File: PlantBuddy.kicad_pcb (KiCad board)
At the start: 4 copper layers, 44.3 x 29.2 mm, 75 parts, among them J1 USB_C_Receptacle_USB2.0, J101 JST, J102 J-Link SWD, J4 External, Q101 DMG1012T, SW1 SW_Push, U1 LTR-303ALS-01, U101 RT9080-33GJ5, U102 nRF52832-QFAA, U104 XB5350A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

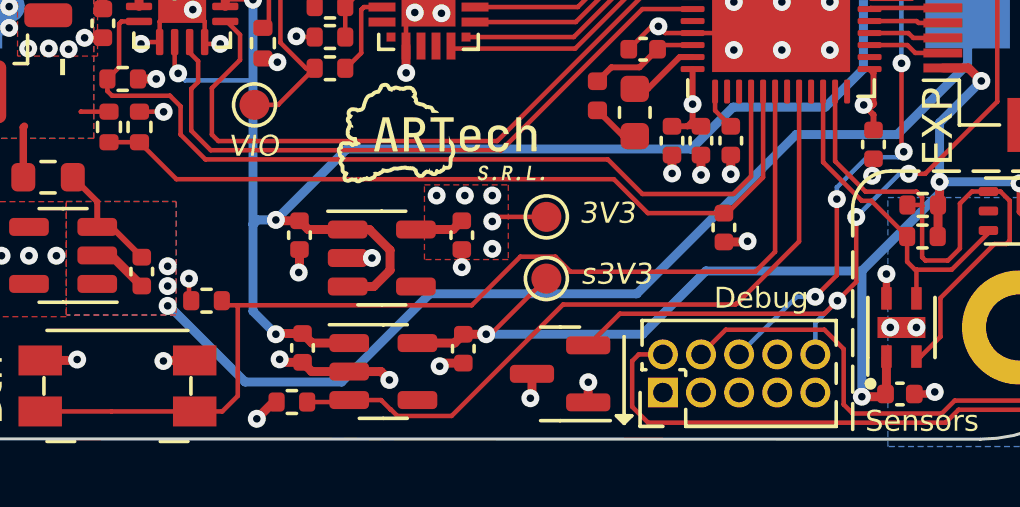
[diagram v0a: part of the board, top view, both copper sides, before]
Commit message: Added voltage monitoring IC. Shuts everything down if Vbat < 3V
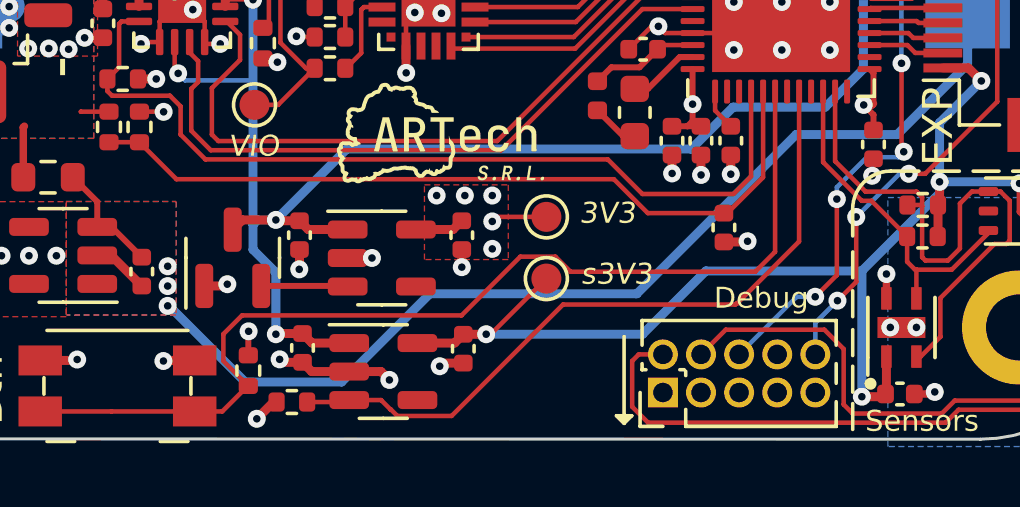
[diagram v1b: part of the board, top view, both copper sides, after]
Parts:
- U105: value CN809R -> CN809T
- moved U105 11.6 mm to (130.2, 136.0), turned to 90 degrees
- moved R108 2.72 mm to (130.7, 139.8), turned to 90 degrees
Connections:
- U105 pad 2: /~{tRST} -> /PWR_EN
- U105 pad 3: +3V3 -> VCC
- U5 pad 3: VCC -> /PWR_EN
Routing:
- net /~{tRST}: track 30.9 -> 21.9 mm
- net /PWR_EN: track 0.00 -> 2.89 mm
- net VCC: track 62.8 -> 60.4 mm
- net +3V3: track 15.3 -> 14.5 mm, vias 10 -> 9

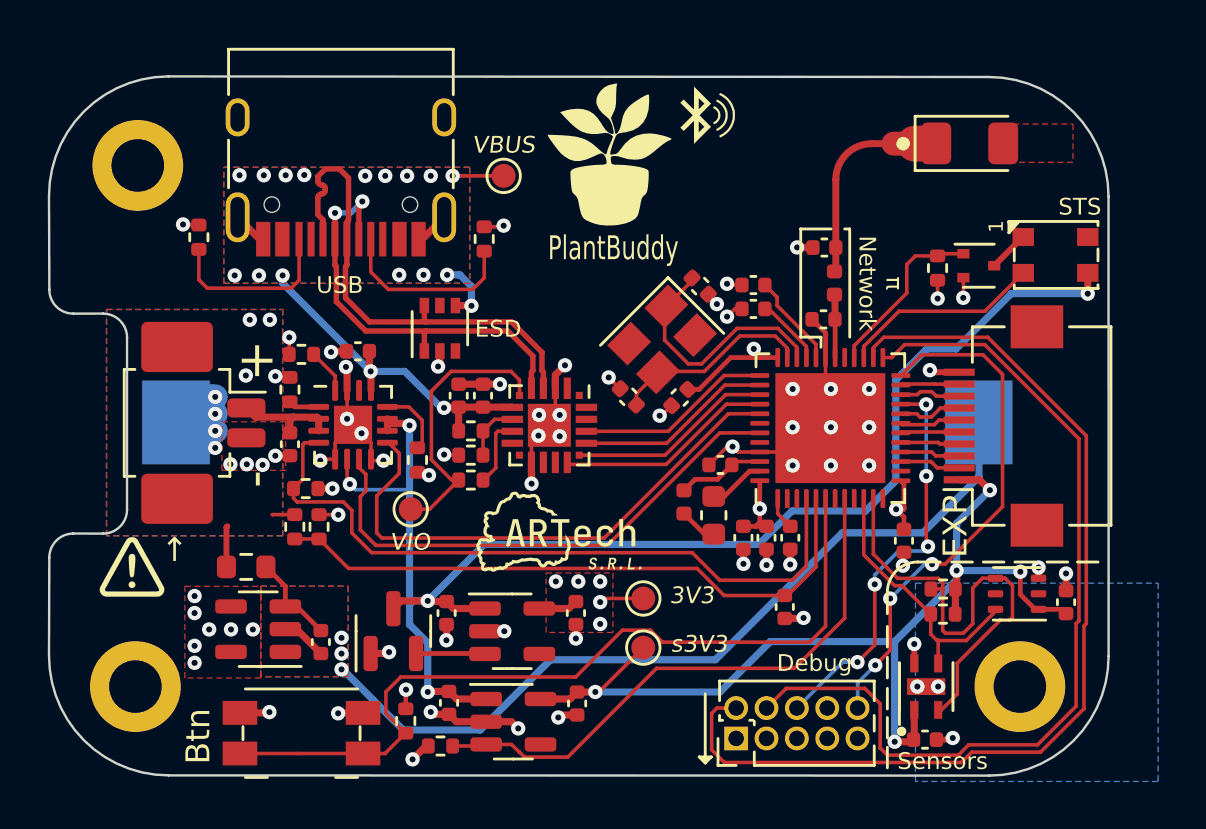
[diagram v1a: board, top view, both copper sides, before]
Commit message: Fixed high power consumption when Vsupply < 3V3
- Added 3V LDO instead of 3.3V LDO.
- Changed RGB LED from Neopixel to simple PWM-based.
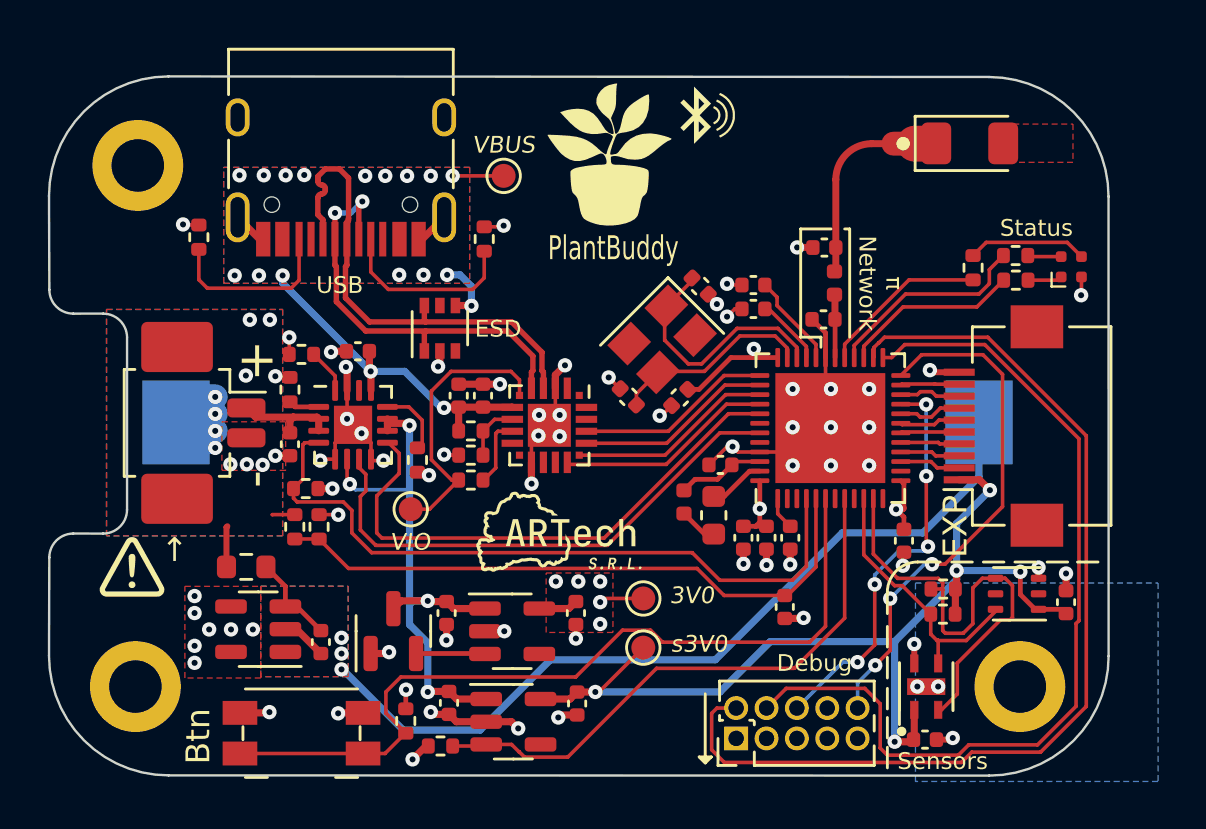
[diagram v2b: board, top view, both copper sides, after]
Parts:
- removed D1: SK6812SMINI-ER, Neopixel:XL-3528RGBW-WS2812B
- removed Q101: DMG1012T, Package_TO_SOT_SMD:SOT-523
- added D102: LED_RGBA, LED_SMD:LED_Lumex_SML-LX0404SIUPGUSB, F.Cu at (158.6, 120.8)
- added R107: 166, Resistor_SMD:R_0402_1005Metric, F.Cu at (154.5, 120.8)
- added R109: 166, Resistor_SMD:R_0402_1005Metric, F.Cu at (156.2, 120.3)
- R102: value 10k -> 433
- TP101: value TP_3V3 -> TP_3V0
- TP102: value TP_s3V3 -> TP_s3V0
- U101, U5: value RT9080-33GJ5 -> ME6231C33M5G
- moved R102 3.31 mm to (156.2, 121.3), turned to 180 degrees
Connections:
- net +3V3 renamed +3V0
- net /S_3V3 renamed /S_3V0
- R102 pad 1: GND -> Net-(D102-Pad1)
- R102 pad 2: /EN_RGB -> /LED_R
- U102 pad 27: /LED_TX -> /LED_R
- U102 pad 28: /EN_RGB -> /LED_G
- U102 pad 29: unconnected-(U102-Pad29) -> /LED_B
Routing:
- net VCC: track 60.4 -> 24.1 mm, vias 5 -> 4
- net /LED_G: track 0.00 -> 8.65 mm
- net /LED_TX: track 8.41 -> 0.00 mm
- net /LED_R: track 0.00 -> 7.47 mm
- net /EN_RGB: track 7.36 -> 0.00 mm
- net /LED_B: track 0.00 -> 7.04 mm
- net Net-(D102-Pad3): track 0.00 -> 5.01 mm
- net Net-(D1-Pad1): track 1.71 -> 0.00 mm
- net GND: track 57.2 -> 55.6 mm, vias 71 -> 69
- net Net-(D102-Pad1): track 0.00 -> 1.44 mm
- net Net-(D102-Pad2): track 0.00 -> 1.41 mm
- net +3V0: track 14.5 -> 15.2 mm, vias 9 -> 10
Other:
- board text added: "3V0"
- board text added: "Status"
- board text added: "s3V0"
- board text removed: "3V3"
- board text removed: "STS"
- board text removed: "s3V3"

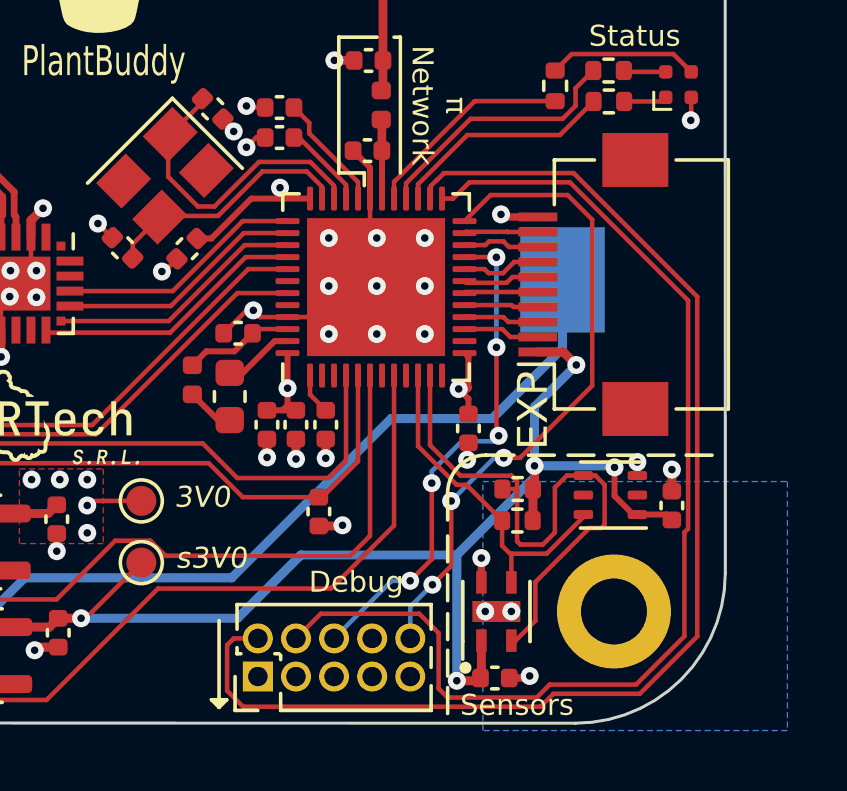
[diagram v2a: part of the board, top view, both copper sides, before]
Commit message: Exchanged debug connector for Tag-Connect TC2030-CTX-NL
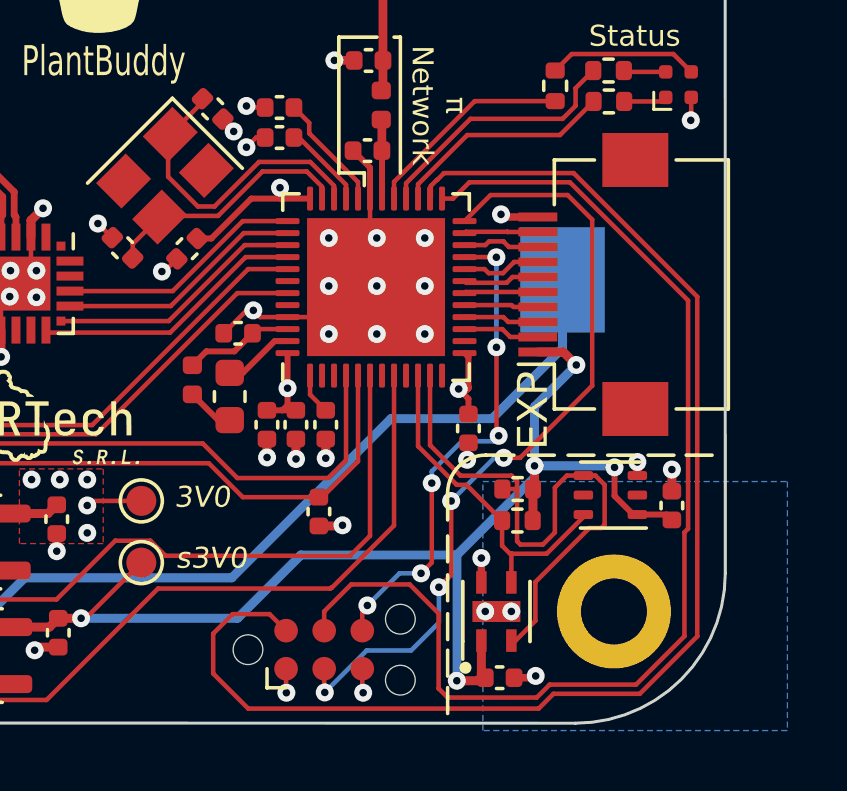
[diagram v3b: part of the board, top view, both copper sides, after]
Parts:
- J102: value J-Link SWD -> Debug; footprint Connector_PinHeader_1.27mm:PinHeader_2x05_P1.27mm_Vertical -> Connector:Tag-Connect_TC2030-IDC-NL_2x03_P1.27mm_Vertical
- R102: value 433 -> 330R
- R107, R109: value 166 -> 120R
- moved J102 2.38 mm to (146.8, 139.6), turned to 0 degrees
- moved C2 0.16 mm to (152.6, 140.5)
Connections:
- J102 pad 3: GND -> /~{tRST}
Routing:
- net /~{tRST}: track 21.9 -> 26.6 mm, vias 3 -> 4
- net /SWDIO: track 42.0 -> 44.4 mm
- net GND: track 55.6 -> 56.5 mm, vias 69 -> 70
- net +3V0: track 15.2 -> 16.0 mm, vias 10 -> 11
- net /SWO: track 17.0 -> 16.5 mm, vias 5 -> 6
- net /SWCLK: track 37.7 -> 38.2 mm
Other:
- board text removed: "Debug"
- board text removed: "Sensors"

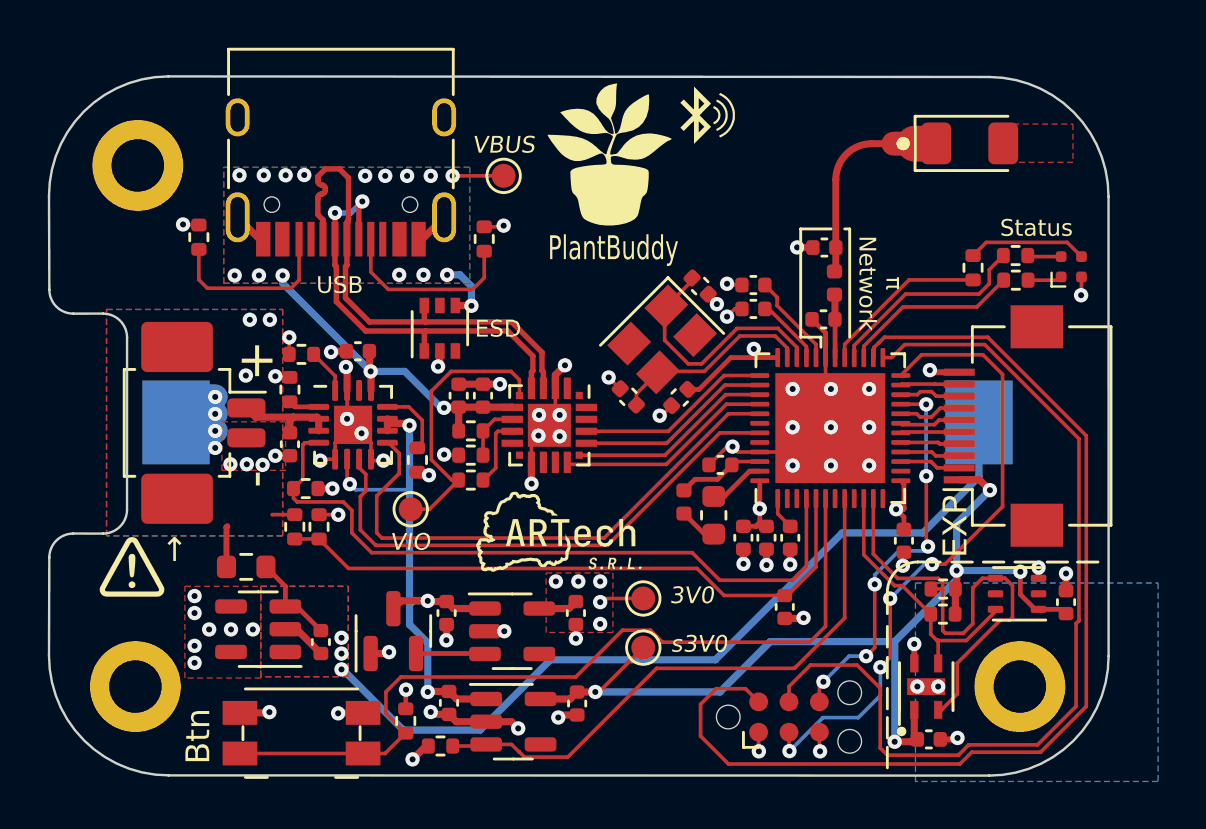
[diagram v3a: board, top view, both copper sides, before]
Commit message: Added JLCPCB tooling holes & moved mounting holes.
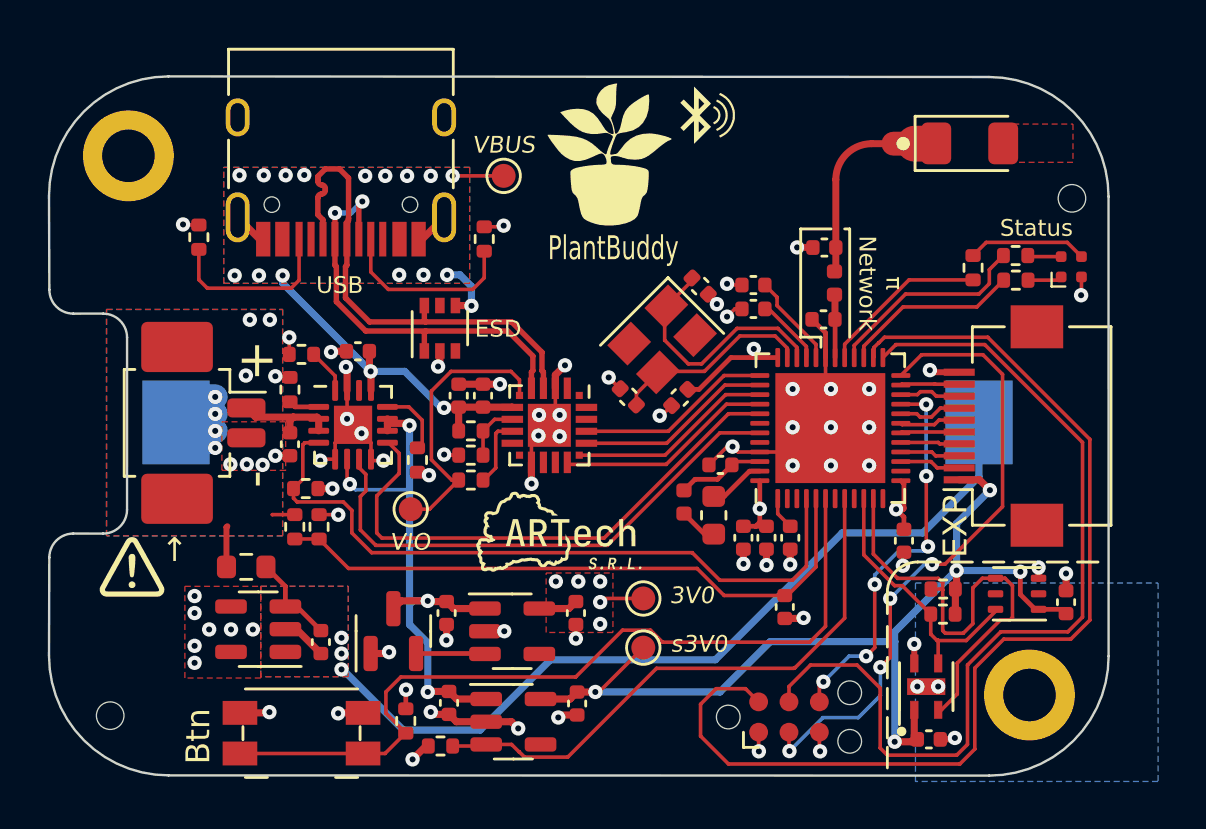
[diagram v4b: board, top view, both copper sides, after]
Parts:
- added H104: ToolingHole, Tooling:JLCPCB_Tooling_hole, F.Cu at (158.6, 117.9)
- H101: value MountingHole -> ToolingHole; footprint MountingHole:MountingHole_2.2mm_M2_DIN965_Pad -> Tooling:JLCPCB_Tooling_hole
- moved H101 1.61 mm to (118.4, 139.5)
- moved H102 0.56 mm to (119.1, 116.1)
- moved H103 0.53 mm to (156.8, 138.7)

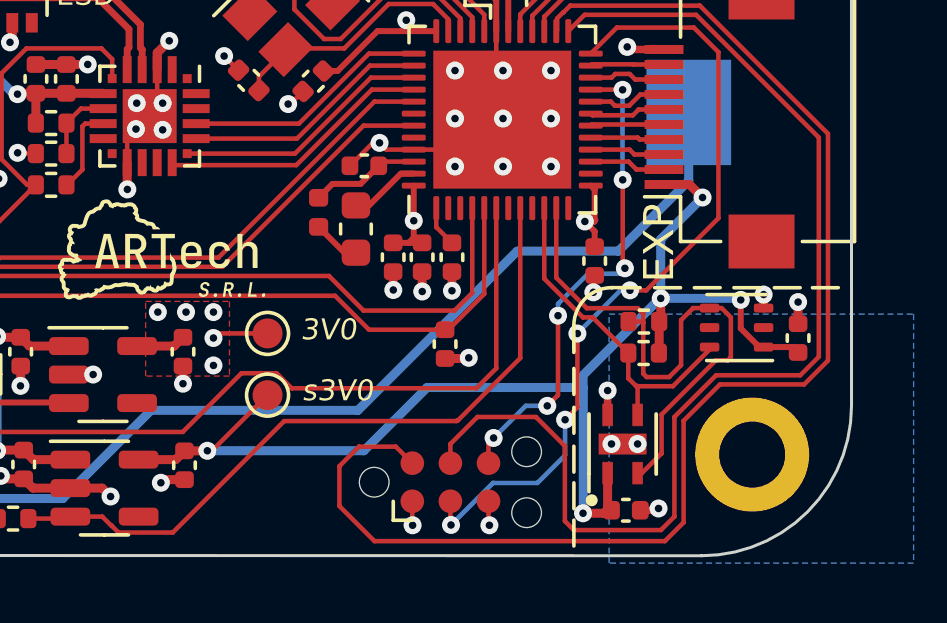
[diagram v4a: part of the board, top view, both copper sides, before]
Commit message: Switched LDO to a better, brand-name one.
- Also am now powering the i2c sensors directly from the LDO because I
noticed current spikes in the previous EN -> measure -> DIS
implementation.
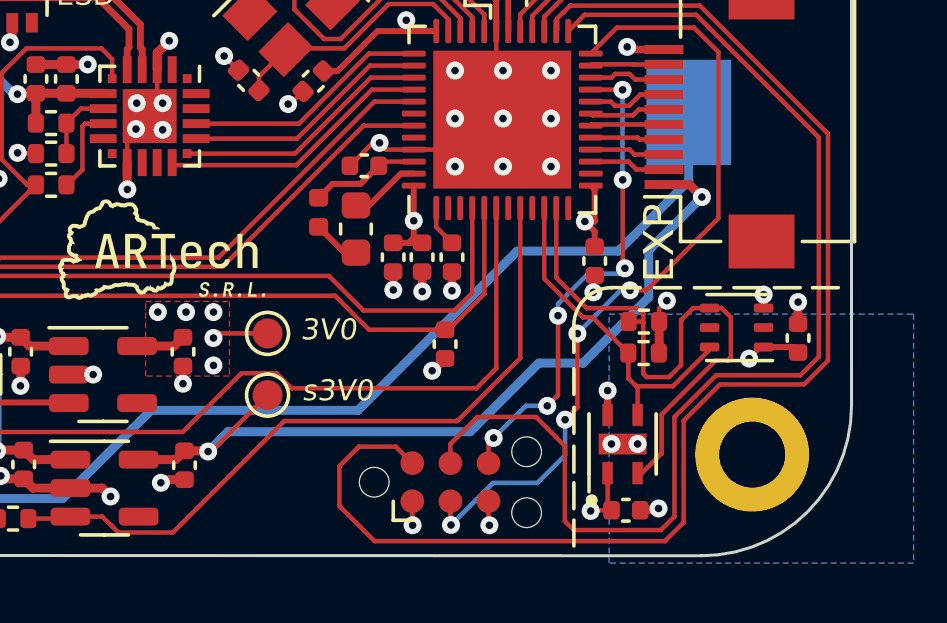
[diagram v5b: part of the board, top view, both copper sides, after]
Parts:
- U101, U5: value ME6231C33M5G -> AP2139AK-3.0TRG1
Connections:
- C1 pad 1: /S_3V0 -> +3V0
- C2 pad 1: /S_3V0 -> +3V0
- R3 pad 2: /S_3V0 -> +3V0
- R4 pad 2: /S_3V0 -> +3V0
- U1 pad 1: /S_3V0 -> +3V0
- U2 pad 1: /S_3V0 -> +3V0
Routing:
- net /S_3V0: track 42.1 -> 27.5 mm, vias 5 -> 2
- net +3V0: track 16.0 -> 21.8 mm, vias 11 -> 14
